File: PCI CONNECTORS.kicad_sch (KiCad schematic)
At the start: 17 parts, among them J34 PCI1, J35 PCI1

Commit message: Pages 16 17 PCI, tweaked page 15
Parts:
- removed J34, J35: PCI1, P2-3_ERA:PCI_GENERIC, symbol P2-3_era:PCI_Generic_1
- added J34, J35: PCI_CONN, custom:PCI1, symbol P2-3_era:PCI_Slot
- C14, C15, C16, C17: value 0.1uf 16v -> 0.1uf
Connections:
- net AD26 is gone; now on net AD0: R62.2
- net AD27 is gone; now on net AD1: R64.2
- net PRSNT11 is gone; now on net PRSNT#11: C14.2
- net PRSNT12 is gone; now on net PRSNT#12: C15.2
- net PRSNT21 is gone; now on net PRSNT#21: C16.2
- net PRSNT22 is gone; now on net PRSNT#22: C17.2
- net AD0: now also J34.A20 (AD(30)), J34.A22 (AD(28)), J34.A23 (AD(26)), J34.A25 (AD(24)), J34.A28 (AD(22)), J34.A29 (AD(20)), J34.A31 (AD(18)), J34.A32 (AD(16)), J34.A44 (AD(15)), J34.A46 (AD(13)), J34.A47 (AD(11)), J34.A49 (AD(09)), J34.A54 (AD(06)), J34.A55 (AD(04)), J34.A57 (AD(02)), J34.A58 (AD(00)), J35.A20 (AD(30)), J35.A22 (AD(28)), J35.A23 (AD(26)), J35.A25 (AD(24)), J35.A28 (AD(22)), J35.A29 (AD(20)), J35.A31 (AD(18)), J35.A32 (AD(16)), J35.A44 (AD(15)), J35.A46 (AD(13)), J35.A47 (AD(11)), J35.A49 (AD(09)), J35.A54 (AD(06)), J35.A55 (AD(04)), J35.A57 (AD(02)), J35.A58 (AD(00))
- net AD1: now also J34.B20 (AD(31)), J34.B21 (AD(29)), J34.B23 (AD(27)), J34.B24 (AD(25)), J34.B27 (AD(23)), J34.B29 (AD(21)), J34.B30 (AD(19)), J34.B32 (AD(17)), J34.B45 (AD(14)), J34.B47 (AD(12)), J34.B48 (AD(10)), J34.B52 (AD(8)), J34.B53 (AD(7)), J34.B55 (AD(5)), J34.B56 (AD(3)), J34.B58 (AD(1)), J35.B20 (AD(31)), J35.B21 (AD(29)), J35.B23 (AD(27)), J35.B24 (AD(25)), J35.B27 (AD(23)), J35.B29 (AD(21)), J35.B30 (AD(19)), J35.B32 (AD(17)), J35.B45 (AD(14)), J35.B47 (AD(12)), J35.B48 (AD(10)), J35.B52 (AD(8)), J35.B53 (AD(7)), J35.B55 (AD(5)), J35.B56 (AD(3)), J35.B58 (AD(1))
- net C/BE#(0): now also J34.A52 (C/BE#(0)), J35.A52 (C/BE#(0))
- net C/BE#(1): now also J34.B26 (C/BE#(3)), J34.B33 (C/BE#(2)), J34.B44 (C/BE#(1)), J35.B26 (C/BE#(3)), J35.B33 (C/BE#(2)), J35.B44 (C/BE#(1))
- net DEVSEL#: now also J34.B37 (DEVSEL#), J35.B37 (DEVSEL#)
- net FRAME#: now also J34.A34 (FRAME#), J35.A34 (FRAME#)
- net IRDY#: now also J34.B35 (IRDY#), J35.B35 (IRDY#)
- net PAR: now also J34.A43 (PAR), J35.A43 (PAR)
- net PCIRST#: now also J34.A15 (RESET#), J35.A15 (RESET#)
- net PCI_PME#: now also J34.A19 (PME#), J35.A19 (PME#)
- net PCLK1: now also J34.B16 (CLK)
- net PCLK2: now also J35.B16 (CLK)
- net PERR#: now also J34.B40 (PERR#), J35.B40 (PERR#)
- net PGNT#1: now also J35.A17 (GNT#)
- net PIRQ#A: now also J34.A6 (INTA#), J35.B8 (INTD#)
- net PIRQ#B: now also J34.B7 (INTB#), J35.A6 (INTA#)
- net PIRQ#C: now also J34.A7 (INTC#), J35.B7 (INTB#)
- net PIRQ#D: now also J34.B8 (INTD#), J35.A7 (INTC#)
- net PLOCK#: now also J34.B39 (LOCK#), J35.B39 (LOCK#)
- net PREQ#0: now also J34.B18 (REQ#)
- net PREQ#1: now also J35.B18 (REQ#)
- net PRSNT#11: now also J34.B9 (PRSNT1#)
- net PRSNT#12: now also J34.B11 (PRSNT2#)
- net PRSNT#21: now also J35.B9 (PRSNT1#)
- net PRSNT#22: now also J35.B11 (PRSNT2#)
- net PTCK: now also J34.B2 (TCK), J35.B2 (TCK)
- net PTDI: now also J34.A4 (TDI), J35.A4 (TDI)
- net PTMS: now also J34.A3 (TMS), J35.A3 (TMS)
- net PTRST#: now also R60.1, J34.A1 (TRST#), J35.A1 (TRST#); no longer R60.2
- net PU1_ACK64#: now also J34.A60 (REQ64#)
- net PU1_REQ64#: now also J34.B60 (ACK64#)
- net PU2_REQ64#: now also J35.B60 (ACK64#)
- net R_AD26: now also J34.A26 (IDSEL)
- net R_AD27: now also J35.A26 (IDSEL)
- net SBOP1: now also J34.A41 (SBO#)
- net SBOP2: now also J35.A41 (SBO#)
- net SDONEP1: now also J34.A40 (SDONE)
- net SDONEP2: now also J35.A40 (SDONE)
- net SERR#: now also J34.B42 (SERR#), J35.B42 (SERR#)
- net STOP#: now also J34.A38 (STOP#), J35.A38 (STOP#)
- net TRDY#: now also J34.A36 (TRDY#), J35.A36 (TRDY#)
- net Earth: no longer names the net of C14.1, C15.1, C16.1, C17.1
- net Earth: no longer R59.1, R60.1, R65.2
- new net: J34.A10 (+5V), J34.A16 (+5V), J34.A5 (+5V), J34.A59 (+5V), J34.A61 (+5V), J34.A62 (+5V), J34.A8 (+5V)
- new net: J34.A21 (+3.3V), J34.A27 (+3.3V), J34.A33 (+3.3V), J34.A39 (+3.3V), J34.A45 (+3.3V), J34.A53 (+3.3V)
- new net: J34.B19 (+5V), J34.B5 (+5V), J34.B59 (+5V), J34.B6 (+5V), J34.B61 (+5V), J34.B62 (+5V)
- new net: J34.B25 (+3.3V), J34.B31 (+3.3V), J34.B36 (+3.3V), J34.B41 (+3.3V), J34.B43 (+3.3V), J34.B54 (+3.3V)
- new net: J35.A10 (+5V), J35.A16 (+5V), J35.A5 (+5V), J35.A59 (+5V), J35.A61 (+5V), J35.A62 (+5V), J35.A8 (+5V)
- new net: J35.A21 (+3.3V), J35.A27 (+3.3V), J35.A33 (+3.3V), J35.A39 (+3.3V), J35.A45 (+3.3V), J35.A53 (+3.3V)
- new net: J35.B19 (+5V), J35.B5 (+5V), J35.B59 (+5V), J35.B6 (+5V), J35.B61 (+5V), J35.B62 (+5V)
- new net: J35.B25 (+3.3V), J35.B31 (+3.3V), J35.B36 (+3.3V), J35.B41 (+3.3V), J35.B43 (+3.3V), J35.B54 (+3.3V)
- new net GND: J34.A12 (GND), J34.A13 (GND), J34.A18 (GND), J34.A24 (GND), J34.A30 (GND), J34.A35 (GND), J34.A37 (GND), J34.A42 (GND), J34.A48 (GND), J34.A56 (GND), J34.B12 (GND), J34.B13 (GND), J34.B15 (GND), J34.B17 (GND), J34.B22 (GND), J34.B28 (GND), J34.B3 (GND), J34.B34 (GND), J34.B38 (GND), J34.B46 (GND), J34.B49 (GND), J34.B57 (GND), J35.A12 (GND), J35.A13 (GND), J35.A18 (GND), J35.A24 (GND), J35.A30 (GND), J35.A35 (GND), J35.A37 (GND), J35.A42 (GND), J35.A48 (GND), J35.A56 (GND), J35.B12 (GND), J35.B13 (GND), J35.B15 (GND), J35.B17 (GND), J35.B22 (GND), J35.B28 (GND), J35.B3 (GND), J35.B34 (GND), J35.B38 (GND), J35.B46 (GND), J35.B49 (GND), J35.B57 (GND), R59.1, R60.2
- new net PGNT#0: J34.A17 (GNT#)
- new net PU2_ACK64#: J35.A60 (REQ64#), R65.2
- no-connect marks 2 -> 12
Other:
- note added: "PCI CONNECTORS 1 AND 2"
- note removed: "PCI SLOTS 1 & 2"
- moved on the sheet: C14, C15, C16, C17, R57, R58, R59, R60, R61, R62, R63, R64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

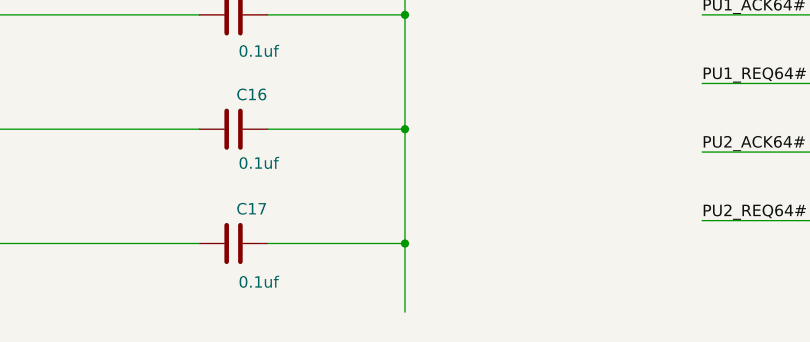
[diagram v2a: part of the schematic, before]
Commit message: page 18 ISA, small fixes
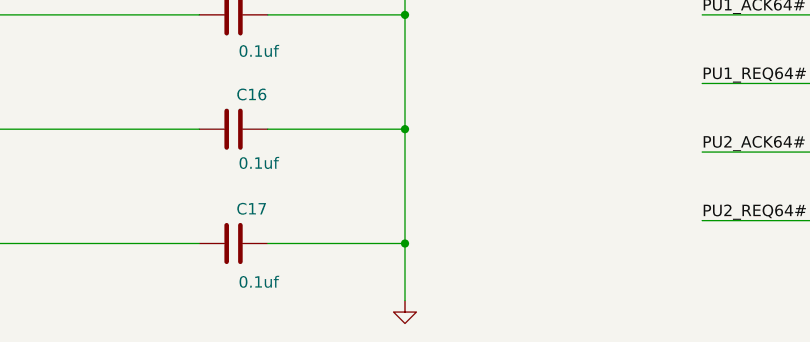
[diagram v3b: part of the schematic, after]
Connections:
- net GND: now also C14.1, C15.1, C16.1, C17.1
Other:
- title: (none) -> PCI CONNECTORS 1 & 2
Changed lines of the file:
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@@
 	(paper "User" 420 340)
 	(title_block
+		(title "PCI CONNECTORS 1 & 2")
 		(date "Thursday, April 09, 1998")
 		(rev "1.0")
@@
 	(wire
 		(pts
-			(xy 187.96 294.64) (xy 187.96 302.26)
+			(xy 187.96 294.64) (xy 187.96 300.99)
 		)
 		(stroke
@@
 					(unit 1)
 				)
+			)
+		)
+	)
+	(symbol
+		(lib_id "power:GND")
+		(at 187.96 300.99 0)
+		(unit 1)
+		(exclude_from_sim no)
+		(in_bom yes)
+		(on_board yes)
+		(dnp no)
+		(fields_autoplaced yes)
+		(property "Reference" "#PWR08072"
+			(at 187.96 307.34 0)
+			(effects
+				(font
+					(size 1.27 1.27)
+				)
+				(hide yes)
+			)
+		)
+		(property "Value" "GND"
+			(at 187.96 306.07 0)
+			(effects
+				(font
+					(size 1.27 1.27)
+				)
+				(hide yes)
+			)
+		)
+		(property "Footprint" ""
+			(at 187.96 300.99 0)
+			(effects
+				(font
+					(size 1.27 1.27)
+				)
+				(hide yes)
+			)
+		)
+		(property "Datasheet" ""
+			(at 187.96 300.99 0)
+			(effects
+				(font
+					(size 1.27 1.27)
+				)
+				(hide yes)
+			)
+		)
+		(property "Description" "Power symbol creates a global label with name \"GND\" , ground"
+			(at 187.96 300.99 0)
+			(effects
+				(font
+					(size 1.27 1.27)
+				)
+				(hide yes)
+			)
+		)
+		(pin "1"
+		)
+		(instances
+			(project "440BX REFERENCE DESIGN"
+				(path "/373c3af7-3bc7-49b4-93d6-3114ef59c408/e4eeeccb-2172-49c5-baf6-923b28080366"
+					(reference "#PWR08072")
+					(unit 1)
+				)

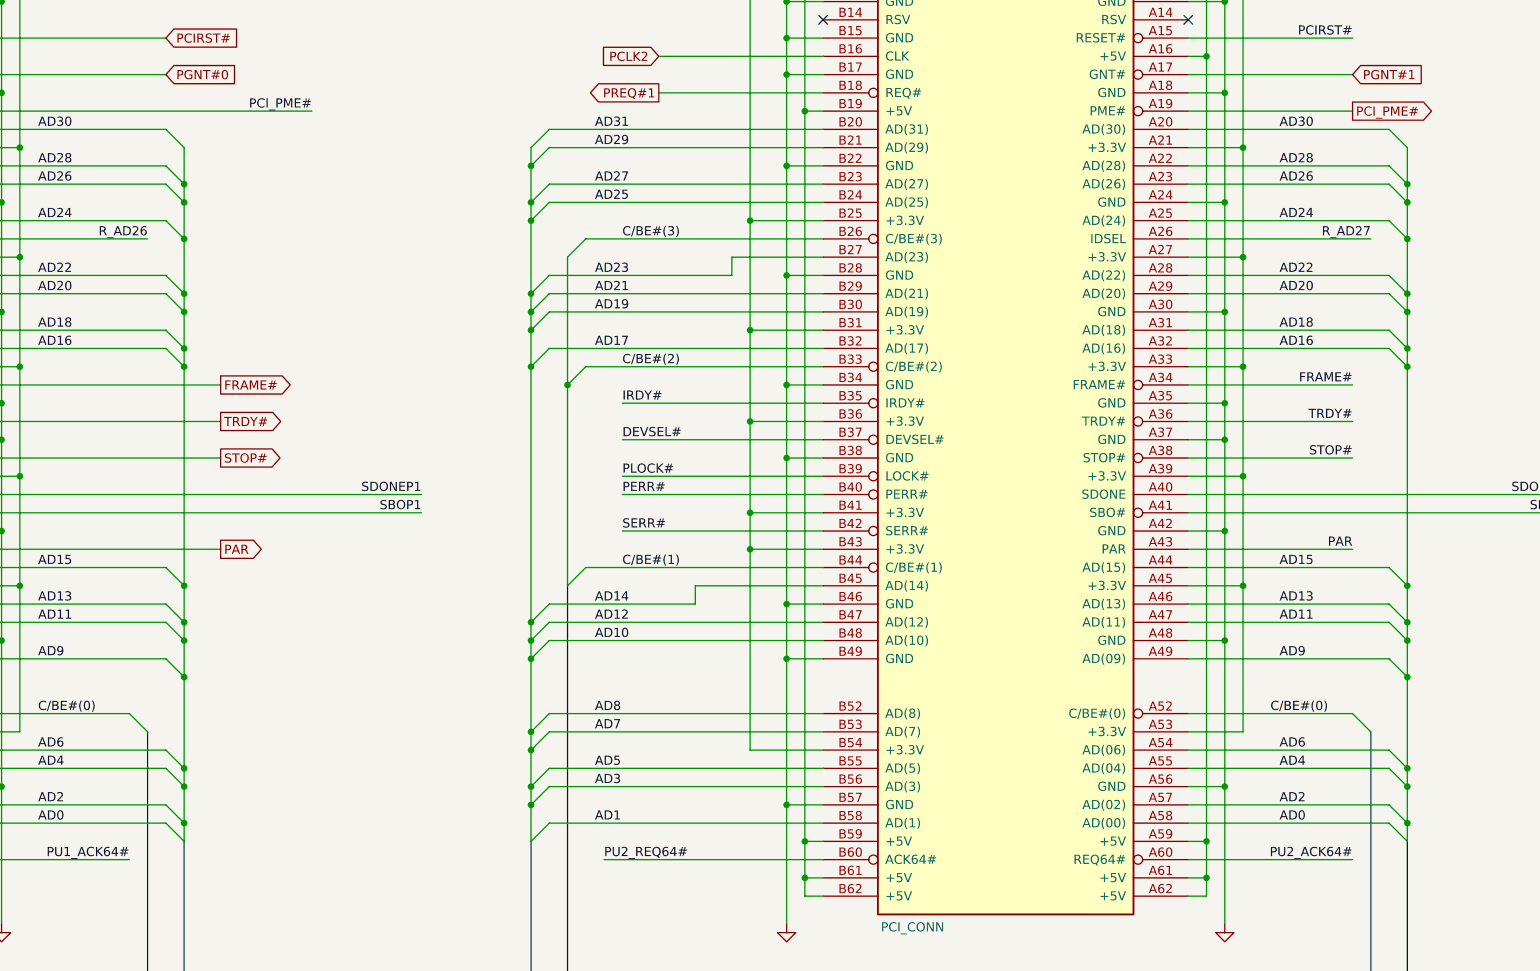
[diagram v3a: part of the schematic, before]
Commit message: page 6,7,8 82443BX chipset, various small fixes
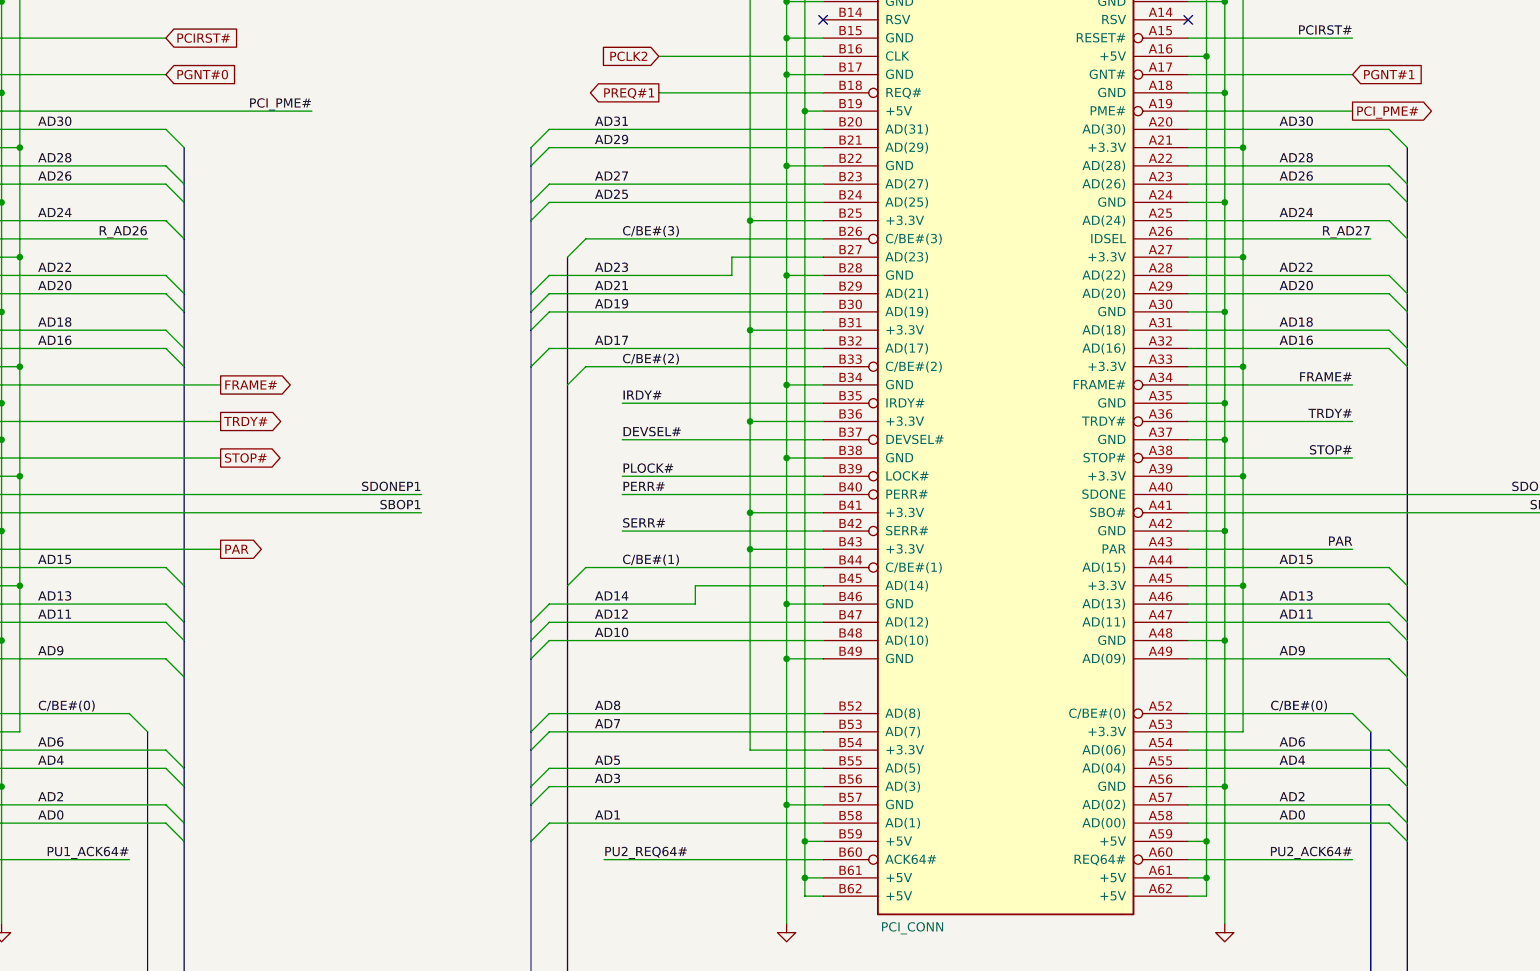
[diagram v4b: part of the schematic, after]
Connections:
- net AD0: no longer J34.A20 (AD(30)), J34.A22 (AD(28)), J34.A23 (AD(26)), J34.A25 (AD(24)), J34.A28 (AD(22)), J34.A29 (AD(20)), J34.A31 (AD(18)), J34.A32 (AD(16)), J34.A44 (AD(15)), J34.A46 (AD(13)), J34.A47 (AD(11)), J34.A49 (AD(09)), J34.A54 (AD(06)), J34.A55 (AD(04)), J34.A57 (AD(02)), J35.A20 (AD(30)), J35.A22 (AD(28)), J35.A23 (AD(26)), J35.A25 (AD(24)), J35.A28 (AD(22)), J35.A29 (AD(20)), J35.A31 (AD(18)), J35.A32 (AD(16)), J35.A44 (AD(15)), J35.A46 (AD(13)), J35.A47 (AD(11)), J35.A49 (AD(09)), J35.A54 (AD(06)), J35.A55 (AD(04)), J35.A57 (AD(02)), R62.2
- net AD1: no longer J34.B20 (AD(31)), J34.B21 (AD(29)), J34.B23 (AD(27)), J34.B24 (AD(25)), J34.B27 (AD(23)), J34.B29 (AD(21)), J34.B30 (AD(19)), J34.B32 (AD(17)), J34.B45 (AD(14)), J34.B47 (AD(12)), J34.B48 (AD(10)), J34.B52 (AD(8)), J34.B53 (AD(7)), J34.B55 (AD(5)), J34.B56 (AD(3)), J35.B20 (AD(31)), J35.B21 (AD(29)), J35.B23 (AD(27)), J35.B24 (AD(25)), J35.B27 (AD(23)), J35.B29 (AD(21)), J35.B30 (AD(19)), J35.B32 (AD(17)), J35.B45 (AD(14)), J35.B47 (AD(12)), J35.B48 (AD(10)), J35.B52 (AD(8)), J35.B53 (AD(7)), J35.B55 (AD(5)), J35.B56 (AD(3)), R64.2
- net C/BE#(1): no longer J34.B26 (C/BE#(3)), J34.B33 (C/BE#(2)), J35.B26 (C/BE#(3)), J35.B33 (C/BE#(2))
- new net AD10: J34.B48 (AD(10)), J35.B48 (AD(10))
- new net AD11: J34.A47 (AD(11)), J35.A47 (AD(11))
- new net AD12: J34.B47 (AD(12)), J35.B47 (AD(12))
- new net AD13: J34.A46 (AD(13)), J35.A46 (AD(13))
- new net AD14: J34.B45 (AD(14)), J35.B45 (AD(14))
- new net AD15: J34.A44 (AD(15)), J35.A44 (AD(15))
- new net AD16: J34.A32 (AD(16)), J35.A32 (AD(16))
- new net AD17: J34.B32 (AD(17)), J35.B32 (AD(17))
- new net AD18: J34.A31 (AD(18)), J35.A31 (AD(18))
- new net AD19: J34.B30 (AD(19)), J35.B30 (AD(19))
- new net AD2: J34.A57 (AD(02)), J35.A57 (AD(02))
- new net AD20: J34.A29 (AD(20)), J35.A29 (AD(20))
- new net AD21: J34.B29 (AD(21)), J35.B29 (AD(21))
- new net AD22: J34.A28 (AD(22)), J35.A28 (AD(22))
- new net AD23: J34.B27 (AD(23)), J35.B27 (AD(23))
- new net AD24: J34.A25 (AD(24)), J35.A25 (AD(24))
- new net AD25: J34.B24 (AD(25)), J35.B24 (AD(25))
- new net AD26: J34.A23 (AD(26)), J35.A23 (AD(26)), R62.2
- new net AD27: J34.B23 (AD(27)), J35.B23 (AD(27)), R64.2
- new net AD28: J34.A22 (AD(28)), J35.A22 (AD(28))
- new net AD29: J34.B21 (AD(29)), J35.B21 (AD(29))
- new net AD3: J34.B56 (AD(3)), J35.B56 (AD(3))
- new net AD30: J34.A20 (AD(30)), J35.A20 (AD(30))
- new net AD31: J34.B20 (AD(31)), J35.B20 (AD(31))
- new net AD4: J34.A55 (AD(04)), J35.A55 (AD(04))
- new net AD5: J34.B55 (AD(5)), J35.B55 (AD(5))
- new net AD6: J34.A54 (AD(06)), J35.A54 (AD(06))
- new net AD7: J34.B53 (AD(7)), J35.B53 (AD(7))
- new net AD8: J34.B52 (AD(8)), J35.B52 (AD(8))
- new net AD9: J34.A49 (AD(09)), J35.A49 (AD(09))
- new net C/BE#(2): J34.B33 (C/BE#(2)), J35.B33 (C/BE#(2))
- new net C/BE#(3): J34.B26 (C/BE#(3)), J35.B26 (C/BE#(3))
